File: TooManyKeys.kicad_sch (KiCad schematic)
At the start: 81 parts, among them U2 TLV61070ADBV, U3 SN74LV1T126DBVR

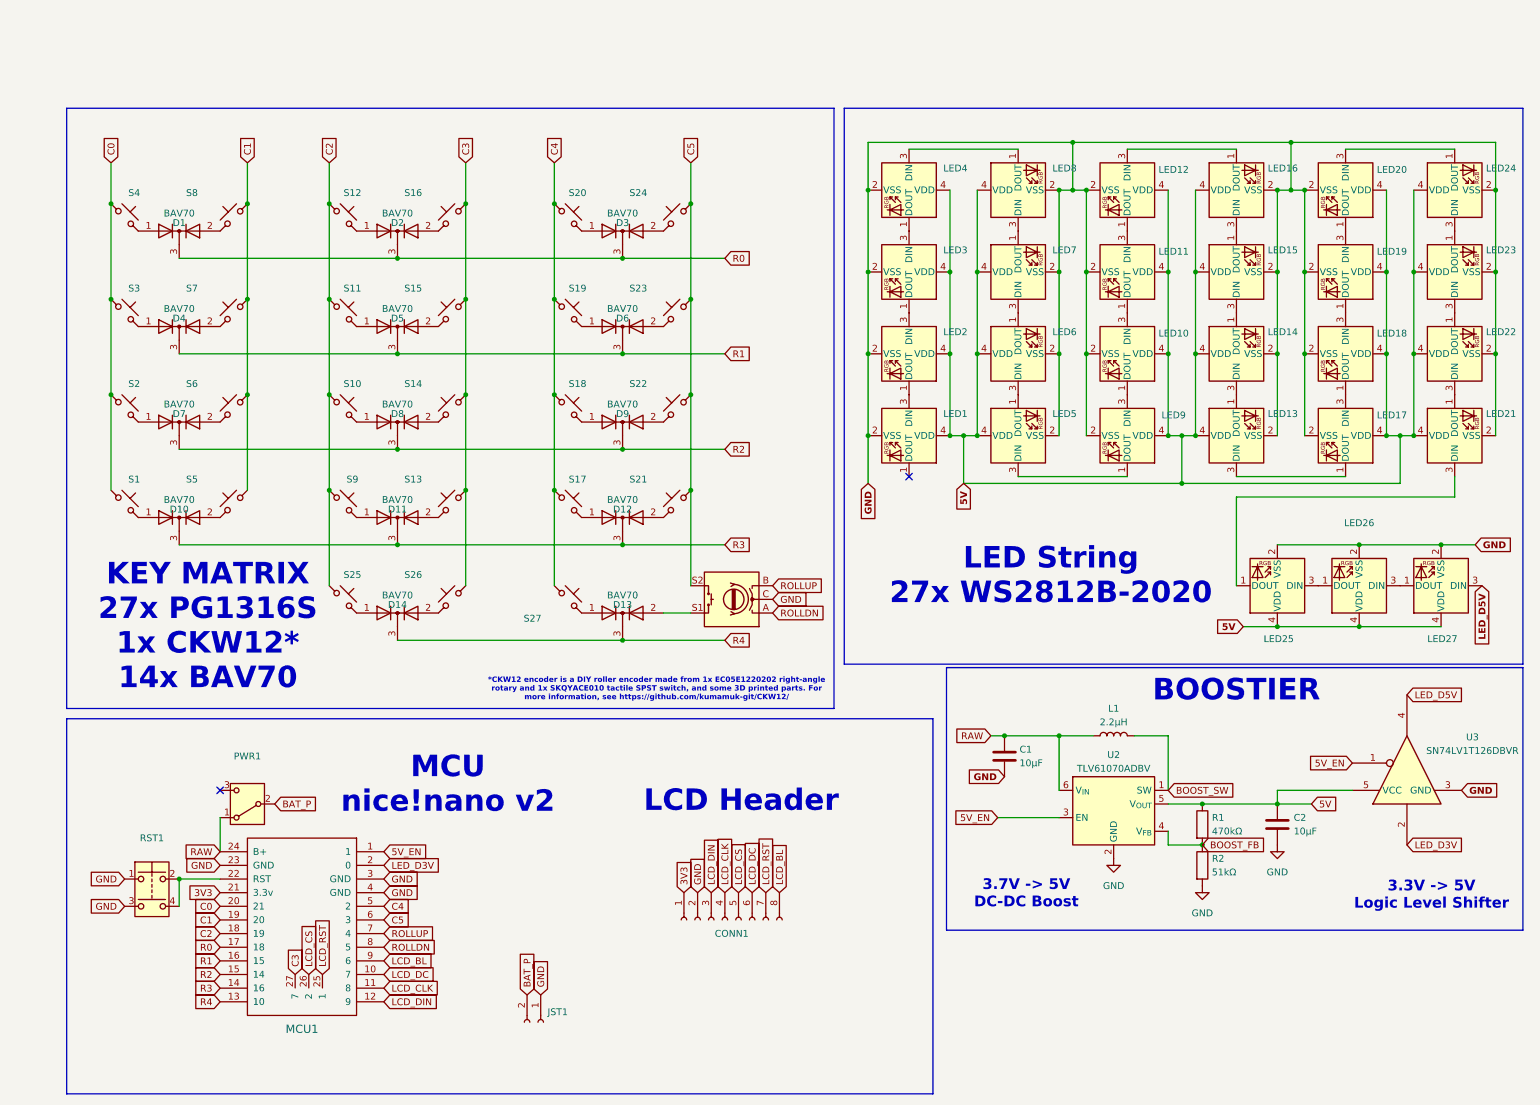
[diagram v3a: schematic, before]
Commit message: Finish clean routing. Attempted sync of schematic failed, but board LGTM and passes DRC other than CKW12 edge issues of no concern.
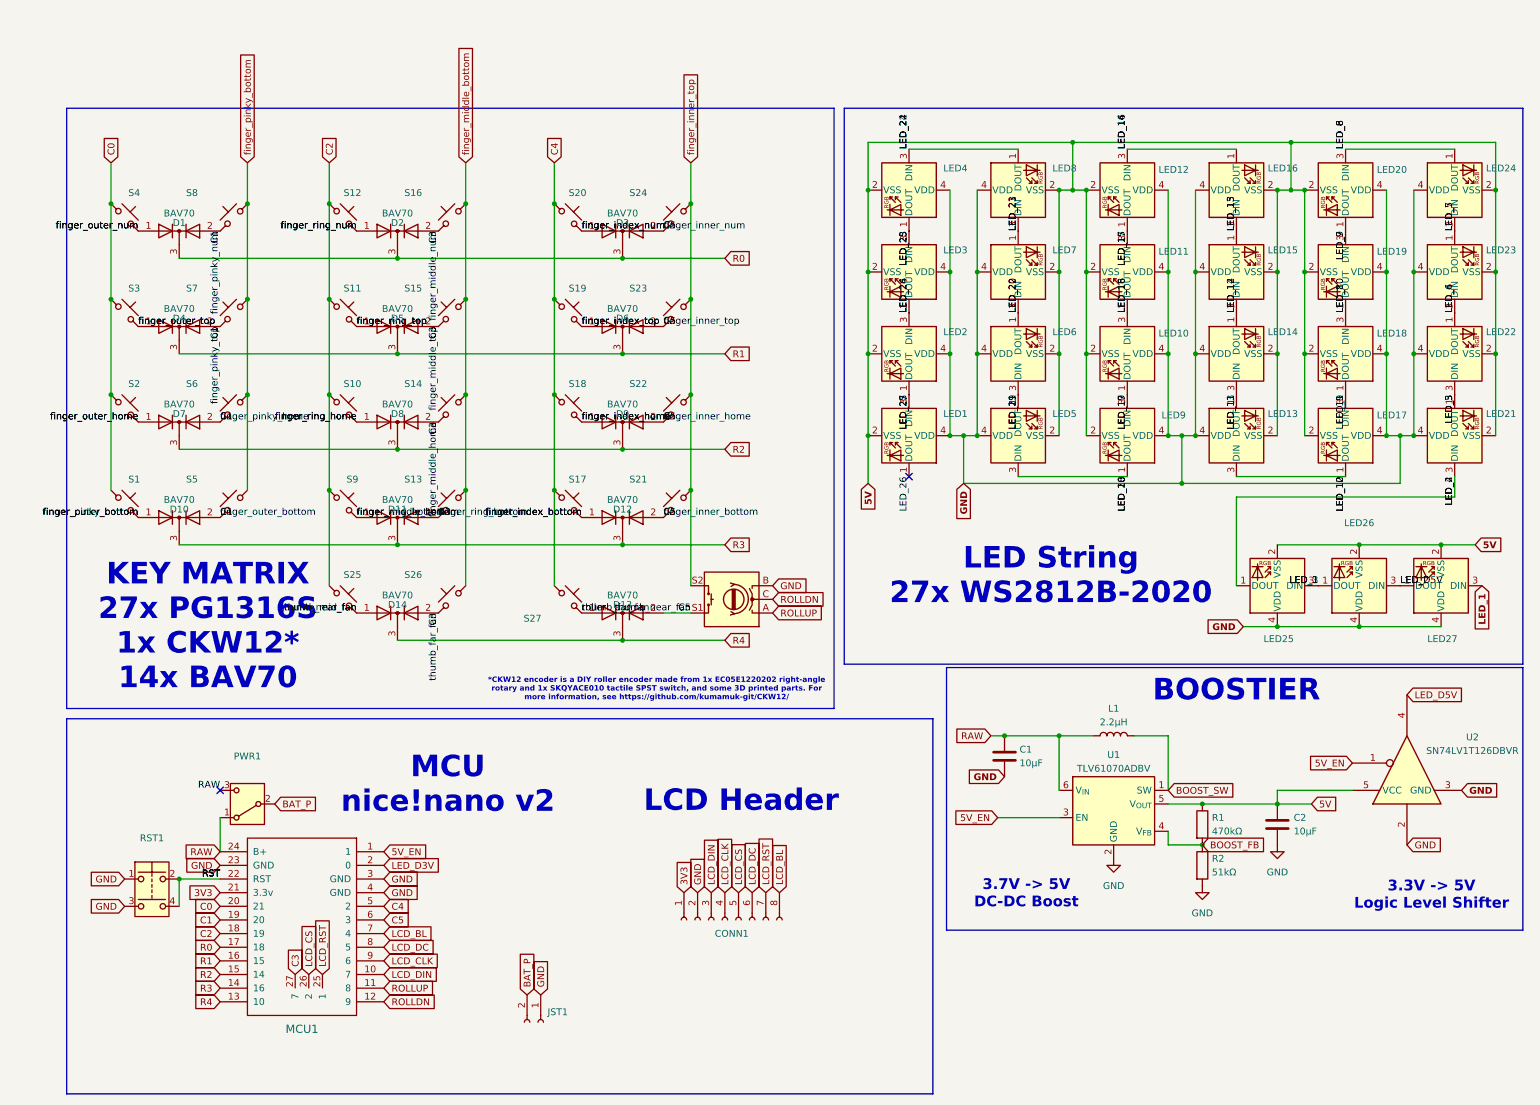
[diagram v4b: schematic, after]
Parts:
- RE1: value (none) -> ~
- renumbered U2 to U1, U3 to U2
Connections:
- net 5V: now also LED1.2 (VSS), LED10.2 (VSS), LED11.2 (VSS), LED12.2 (VSS), LED13.2 (VSS), LED14.2 (VSS), LED15.2 (VSS), LED16.2 (VSS), LED17.2 (VSS), LED18.2 (VSS), LED19.2 (VSS), LED2.2 (VSS), LED20.2 (VSS), LED21.2 (VSS), LED22.2 (VSS), LED23.2 (VSS), LED24.2 (VSS), LED25.2 (VSS), LED26.2 (VSS), LED27.2 (VSS), LED3.2 (VSS), LED4.2 (VSS), LED5.2 (VSS), LED6.2 (VSS), LED7.2 (VSS), LED8.2 (VSS), LED9.2 (VSS); no longer LED1.4 (VDD), LED10.4 (VDD), LED11.4 (VDD), LED12.4 (VDD), LED13.4 (VDD), LED14.4 (VDD), LED15.4 (VDD), LED16.4 (VDD), LED17.4 (VDD), LED18.4 (VDD), LED19.4 (VDD), LED2.4 (VDD), LED20.4 (VDD), LED21.4 (VDD), LED22.4 (VDD), LED23.4 (VDD), LED24.4 (VDD), LED25.4 (VDD), LED26.4 (VDD), LED27.4 (VDD), LED3.4 (VDD), LED4.4 (VDD), LED5.4 (VDD), LED6.4 (VDD), LED7.4 (VDD), LED8.4 (VDD), LED9.4 (VDD)
- net C1: now also D1.2 (A), D10.1 (A), D10.2 (A), D4.2 (A), D7.2 (A), S1.2, S5.1, S6.1, S7.1, S8.1
- net C3: now also D11.1 (A), D11.2 (A), D13.1 (A), D14.2 (A), D2.2 (A), D5.2 (A), D8.2 (A), S13.1, S14.1, S15.1, S16.1, S26.1, S27.2, S9.2
- net C5: now also D12.2 (A), D13.2 (A), D14.1 (A), D3.2 (A), D6.2 (A), D9.2 (A), RE1.S1, S21.1, S22.1, S23.1, S24.1, S25.2
- net GND: now also LED1.4 (VDD), LED10.4 (VDD), LED11.4 (VDD), LED12.4 (VDD), LED13.4 (VDD), LED14.4 (VDD), LED15.4 (VDD), LED16.4 (VDD), LED17.4 (VDD), LED18.4 (VDD), LED19.4 (VDD), LED2.4 (VDD), LED20.4 (VDD), LED21.4 (VDD), LED22.4 (VDD), LED23.4 (VDD), LED24.4 (VDD), LED25.4 (VDD), LED26.4 (VDD), LED27.4 (VDD), LED3.4 (VDD), LED4.4 (VDD), LED5.4 (VDD), LED6.4 (VDD), LED7.4 (VDD), LED8.4 (VDD), LED9.4 (VDD), RE1.B, U2.2; no longer LED1.2 (VSS), LED10.2 (VSS), LED11.2 (VSS), LED12.2 (VSS), LED13.2 (VSS), LED14.2 (VSS), LED15.2 (VSS), LED16.2 (VSS), LED17.2 (VSS), LED18.2 (VSS), LED19.2 (VSS), LED2.2 (VSS), LED20.2 (VSS), LED21.2 (VSS), LED22.2 (VSS), LED23.2 (VSS), LED24.2 (VSS), LED25.2 (VSS), LED26.2 (VSS), LED27.2 (VSS), LED3.2 (VSS), LED4.2 (VSS), LED5.2 (VSS), LED6.2 (VSS), LED7.2 (VSS), LED8.2 (VSS), LED9.2 (VSS), RE1.C
- net LCD_BL: now also MCU1.7 (4); no longer MCU1.9 (6)
- net LCD_CLK: now also MCU1.9 (6); no longer MCU1.11 (8)
- net LCD_DC: now also MCU1.8 (5); no longer MCU1.10 (7)
- net LCD_DIN: now also MCU1.10 (7); no longer MCU1.12 (9)
- net LED_D3V: no longer U2.2
- net LED_D5V: now also LED1.1 (DOUT), LED10.3 (DIN), LED11.1 (DOUT), LED12.3 (DIN), LED13.3 (DIN), LED14.1 (DOUT), LED15.3 (DIN), LED16.1 (DOUT), LED17.1 (DOUT), LED18.3 (DIN), LED19.1 (DOUT), LED2.3 (DIN), LED20.3 (DIN), LED21.3 (DIN), LED22.1 (DOUT), LED23.3 (DIN), LED24.1 (DOUT), LED25.1 (DOUT), LED26.3 (DIN), LED27.1 (DOUT), LED3.1 (DOUT), LED4.3 (DIN), LED5.3 (DIN), LED6.1 (DOUT), LED7.3 (DIN), LED8.1 (DOUT), LED9.1 (DOUT); no longer LED27.3 (DIN)
- net RAW: now also PWR1.3 (C)
- net ROLLDN: now also MCU1.12 (9), RE1.C; no longer MCU1.8 (5), RE1.A
- net ROLLUP: now also MCU1.11 (8), RE1.A; no longer MCU1.7 (4), RE1.B
- net finger_index_bottom: now reaches D12.1 (A), S17.2
- net LED_1: now reaches LED5.1 (DOUT), LED6.3 (DIN)
- net LED_1: now also LED1.3 (DIN), LED10.1 (DOUT), LED11.3 (DIN), LED12.1 (DOUT), LED13.1 (DOUT), LED14.3 (DIN), LED15.1 (DOUT), LED16.3 (DIN), LED17.3 (DIN), LED18.1 (DOUT), LED19.3 (DIN), LED2.1 (DOUT), LED20.1 (DOUT), LED21.1 (DOUT), LED22.3 (DIN), LED23.1 (DOUT), LED24.3 (DIN), LED25.3 (DIN), LED26.1 (DOUT), LED27.3 (DIN), LED3.3 (DIN), LED4.1 (DOUT), LED7.1 (DOUT), LED8.3 (DIN), LED9.3 (DIN)
- net finger_ring_home: now reaches D8.1 (A), S10.2
- net finger_outer_top: now reaches D4.1 (A), S3.2
- net finger_outer_num: now reaches D1.1 (A), S4.2
- net finger_outer_home: now reaches D7.1 (A), S2.2
- net finger_index_home: now reaches D9.1 (A), S18.2
- net finger_index_top: now reaches D6.1 (A), S19.2
- net finger_index_num: now reaches D3.1 (A), S20.2
- net RST: now reaches MCU1.22 (RST), RST1.2, RST1.4
- net finger_ring_top: now reaches D5.1 (A), S11.2
- net finger_ring_num: now reaches D2.1 (A), S12.2

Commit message: wtfO
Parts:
- removed S1, S10, S11, S12, S13, S14, S15, S16, S17, S18, S19, S2, S20, S21, S22, S23, S24, S25, S26, S27, S3, S4, S5, S6, S7, S8, S9: ~, PG1316S, symbol marbastlib-choc:choc_v1_SW_solder
- added S1, S10, S11, S12, S13, S14, S15, S16, S17, S18, S19, S2, S20, S21, S22, S23, S24, S25, S26, S27, S3, S4, S5, S6, S7, S8, S9: ~, PG1316S, symbol huntercooh:PG1316S
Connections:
- net C0: now also S1.1, S6.1, S7.1, S8.1
- net C1: now also S2.1, S3.1, S4.1, S5.1; no longer D1.2 (A), D10.1 (A), D10.2 (A), D4.2 (A), D7.2 (A)
- net C2: now also S14.1, S15.1, S16.1, S25.1, S9.1
- net C3: now also S10.1, S11.1, S12.1, S13.1, S26.1; no longer D11.1 (A), D11.2 (A), D13.1 (A), D14.2 (A), D2.2 (A), D5.2 (A), D8.2 (A)
- net C4: now also S17.1, S18.1, S19.1, S20.1, S27.1
- net C5: now also S21.1, S22.1, S23.1, S24.1; no longer D12.2 (A), D13.2 (A), D14.1 (A), D3.2 (A), D6.2 (A), D9.2 (A), RE1.S2
- net GND: now also LED1.2 (VSS), LED10.2 (VSS), LED11.2 (VSS), LED12.2 (VSS), LED13.2 (VSS), LED14.2 (VSS), LED15.2 (VSS), LED16.2 (VSS), LED17.2 (VSS), LED18.2 (VSS), LED19.2 (VSS), LED2.2 (VSS), LED20.2 (VSS), LED21.2 (VSS), LED22.2 (VSS), LED23.2 (VSS), LED24.2 (VSS), LED25.2 (VSS), LED26.2 (VSS), LED27.2 (VSS), LED3.2 (VSS), LED4.2 (VSS), LED5.2 (VSS), LED6.2 (VSS), LED7.2 (VSS), LED8.2 (VSS), LED9.2 (VSS), RE1.C, S1.3 (B), S10.3 (B), S11.3 (B), S12.3 (B), S13.3 (B), S14.3 (B), S15.3 (B), S16.3 (B), S17.3 (B), S18.3 (B), S19.3 (B), S2.3 (B), S20.3 (B), S21.3 (B), S22.3 (B), S23.3 (B), S24.3 (B), S25.3 (B), S26.3 (B), S27.3 (B), S3.3 (B), S4.3 (B), S5.3 (B), S6.3 (B), S7.3 (B), S8.3 (B), S9.3 (B); no longer LED1.4 (VDD), LED10.4 (VDD), LED11.4 (VDD), LED12.4 (VDD), LED13.4 (VDD), LED14.4 (VDD), LED15.4 (VDD), LED16.4 (VDD), LED17.4 (VDD), LED18.4 (VDD), LED19.4 (VDD), LED2.4 (VDD), LED20.4 (VDD), LED21.4 (VDD), LED22.4 (VDD), LED23.4 (VDD), LED24.4 (VDD), LED25.4 (VDD), LED26.4 (VDD), LED27.4 (VDD), LED3.4 (VDD), LED4.4 (VDD), LED5.4 (VDD), LED6.4 (VDD), LED7.4 (VDD), LED8.4 (VDD), LED9.4 (VDD), U2.2
- net LED_1: no longer LED1.3 (DIN), LED10.1 (DOUT), LED11.3 (DIN), LED12.1 (DOUT), LED13.1 (DOUT), LED14.3 (DIN), LED15.1 (DOUT), LED16.3 (DIN), LED17.3 (DIN), LED18.1 (DOUT), LED19.3 (DIN), LED2.1 (DOUT), LED20.1 (DOUT), LED3.3 (DIN), LED4.1 (DOUT), LED5.1 (DOUT), LED6.3 (DIN), LED7.1 (DOUT), LED8.3 (DIN), LED9.3 (DIN)
- net LED_D3V: now also U2.2
- net LED_D5V: no longer LED1.1 (DOUT), LED10.3 (DIN), LED11.1 (DOUT), LED12.3 (DIN), LED13.3 (DIN), LED14.1 (DOUT), LED15.3 (DIN), LED16.1 (DOUT), LED17.1 (DOUT), LED18.3 (DIN), LED19.1 (DOUT), LED2.3 (DIN), LED20.3 (DIN), LED21.3 (DIN), LED22.1 (DOUT), LED23.3 (DIN), LED24.1 (DOUT), LED25.1 (DOUT), LED26.3 (DIN), LED27.1 (DOUT), LED3.1 (DOUT), LED4.3 (DIN), LED5.3 (DIN), LED6.1 (DOUT), LED7.3 (DIN), LED8.1 (DOUT), LED9.1 (DOUT)
- net RAW: no longer C1.1, L1.1, PWR1.1 (A), U1.6 (V_{IN})
- net ROLLDN: no longer RE1.C
- net finger_index_bottom: now also S17.2
- net finger_index_home: now also S18.2
- net finger_index_num: now also S20.2
- net finger_index_top: now also S19.2
- net finger_outer_home: now also S2.2
- net finger_outer_num: now also S4.2
- net finger_outer_top: now also S3.2
- net finger_ring_home: now also S10.2
- net finger_ring_num: now also S12.2
- net finger_ring_top: now also S11.2
- net 3V3 renamed +3V3
- removed net 5V: C2.1, LED1.2 (VSS), LED10.2 (VSS), LED11.2 (VSS), LED12.2 (VSS), LED13.2 (VSS), LED14.2 (VSS), LED15.2 (VSS), LED16.2 (VSS), LED17.2 (VSS), LED18.2 (VSS), LED19.2 (VSS), LED2.2 (VSS), LED20.2 (VSS), LED21.2 (VSS), LED22.2 (VSS), LED23.2 (VSS), LED24.2 (VSS), LED25.2 (VSS), LED26.2 (VSS), LED27.2 (VSS), LED3.2 (VSS), LED4.2 (VSS), LED5.2 (VSS), LED6.2 (VSS), LED7.2 (VSS), LED8.2 (VSS), LED9.2 (VSS), R1.1, U1.5 (V_{OUT}), U2.5 (VCC)
- net BAT_P renamed +BATT
- net +BATT: now also C1.1, L1.1, U1.6 (V_{IN})
- new net: D14.1 (A), RE1.S2
- new net: D14.2 (A), S25.2
- new net: D13.1 (A), S26.2
- new net: D13.2 (A), S27.2
- new net +5V: C2.1, LED1.4 (VDD), LED10.4 (VDD), LED11.4 (VDD), LED12.4 (VDD), LED13.4 (VDD), LED14.4 (VDD), LED15.4 (VDD), LED16.4 (VDD), LED17.4 (VDD), LED18.4 (VDD), LED19.4 (VDD), LED2.4 (VDD), LED20.4 (VDD), LED21.4 (VDD), LED22.4 (VDD), LED23.4 (VDD), LED24.4 (VDD), LED25.4 (VDD), LED26.4 (VDD), LED27.4 (VDD), LED3.4 (VDD), LED4.4 (VDD), LED5.4 (VDD), LED6.4 (VDD), LED7.4 (VDD), LED8.4 (VDD), LED9.4 (VDD), R1.1, U1.5 (V_{OUT}), U2.5 (VCC)
- new net LED_10: LED13.3 (DIN), LED17.1 (DOUT), LED18.3 (DIN), LED19.1 (DOUT), LED20.3 (DIN), LED24.1 (DOUT)
- new net LED_11: LED17.3 (DIN), LED18.1 (DOUT), LED19.3 (DIN), LED20.1 (DOUT)
- new net LED_12: LED10.3 (DIN), LED11.1 (DOUT), LED12.3 (DIN), LED14.1 (DOUT), LED15.3 (DIN), LED16.1 (DOUT), LED5.3 (DIN), LED9.1 (DOUT)
- new net LED_13: LED10.1 (DOUT), LED11.3 (DIN), LED12.1 (DOUT), LED13.1 (DOUT), LED14.3 (DIN), LED15.1 (DOUT), LED16.3 (DIN), LED9.3 (DIN)
- new net LED_2: LED26.3 (DIN), LED27.1 (DOUT)
- new net LED_20: LED6.1 (DOUT), LED7.3 (DIN)
- new net LED_21: LED3.3 (DIN), LED4.1 (DOUT), LED5.1 (DOUT), LED6.3 (DIN), LED7.1 (DOUT), LED8.3 (DIN)
- new net LED_24: LED4.3 (DIN), LED8.1 (DOUT)
- new net LED_26: LED1.1 (DOUT), LED2.3 (DIN), LED3.1 (DOUT)
- new net LED_27: LED1.3 (DIN), LED2.1 (DOUT)
- new net LED_4: LED21.3 (DIN), LED25.1 (DOUT)
- new net LED_6: LED22.1 (DOUT), LED23.3 (DIN)
- new net finger_inner_bottom: D12.2 (A), S21.2
- new net finger_inner_home: D9.2 (A), S22.2
- new net finger_inner_num: D3.2 (A), S24.2
- new net finger_inner_top: D6.2 (A), S23.2
- new net finger_middle_bottom: D11.1 (A), S13.2
- new net finger_middle_home: D8.2 (A), S14.2
- new net finger_middle_num: D2.2 (A), S16.2
- new net finger_middle_top: D5.2 (A), S15.2
- new net finger_outer_bottom: D10.2 (A), S1.2
- new net finger_pinky_bottom: D10.1 (A), S5.2
- new net finger_pinky_home: D7.2 (A), S6.2
- new net finger_pinky_num: D1.2 (A), S8.2
- new net finger_pinky_top: D4.2 (A), S7.2
- new net finger_ring_bottom: D11.2 (A), S9.2
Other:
- moved on the sheet: JST1, PWR1, RST1
